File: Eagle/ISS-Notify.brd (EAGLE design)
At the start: 63.5 x 63.5 mm, 54 parts, among them J1 AVRISP, J2 JST2, J3 PROTOSPACE2, SW1 9077-1, SW2 SWITCH, U1 ATMEGA32U4, U2 MCP7940N, U3 TPS63001, U4 MCP73811, U5 TLC5971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

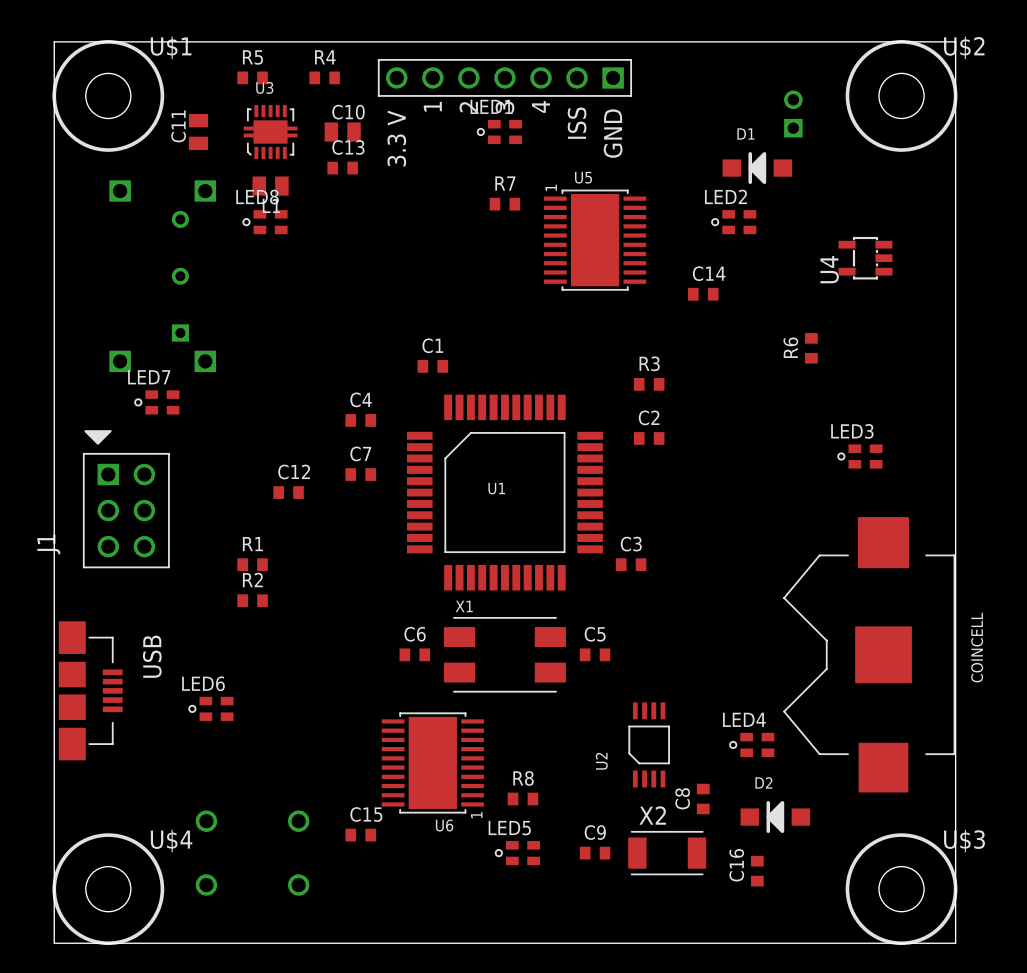
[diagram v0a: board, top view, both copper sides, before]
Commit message: power traces
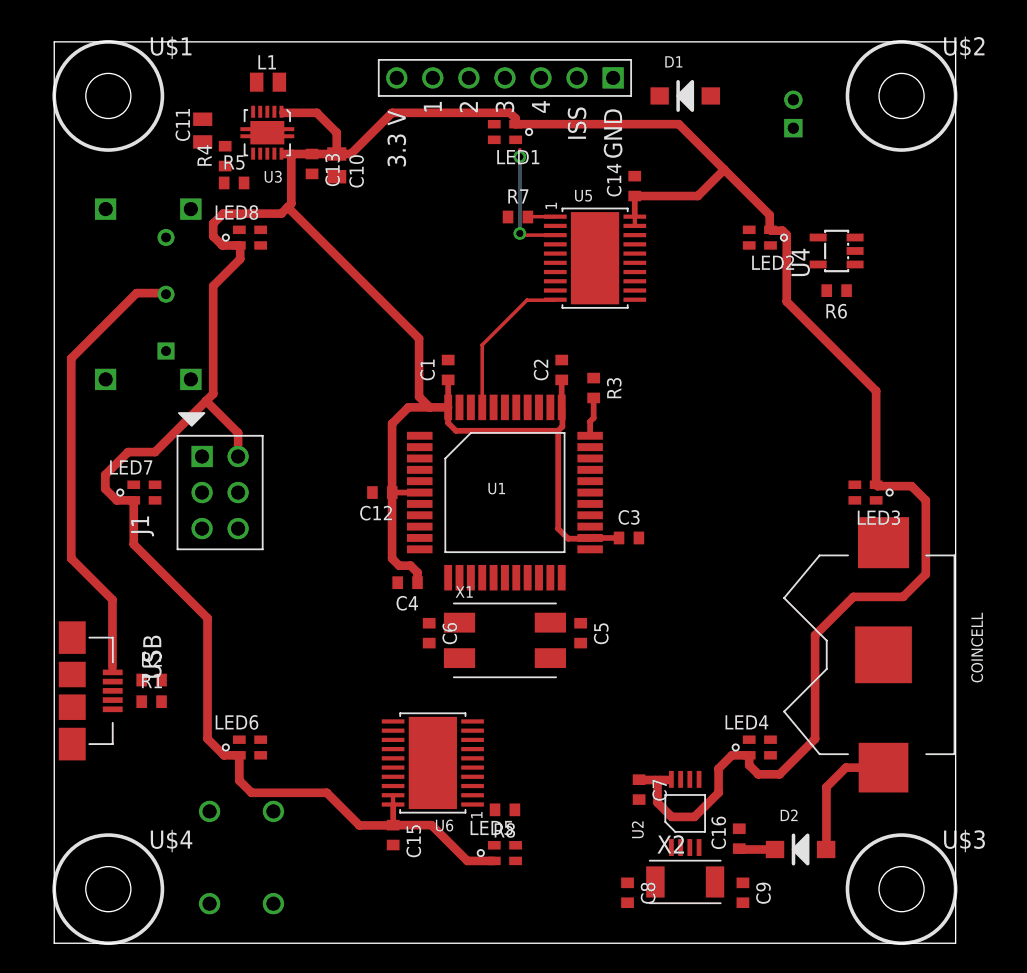
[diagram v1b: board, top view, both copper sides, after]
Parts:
- moved C7 29.6 mm to (41.2, 10.8), turned to 270 degrees
- moved R1 12.0 mm to (6.86, 17.0)
- moved C4 11.9 mm to (24.9, 25.4), turned to 180 degrees
- moved C9 10.8 mm to (48.5, 3.56), turned to 270 degrees
- moved R2 9.04 mm to (6.86, 18.5)
- moved C14 9.02 mm to (40.9, 53.3), turned to 90 degrees
- moved R4 8.92 mm to (12.0, 55.5), turned to 90 degrees
- moved C8 8.49 mm to (40.4, 3.56), turned to 270 degrees
- moved C2 7.83 mm to (35.8, 40.4), turned to 90 degrees
- moved R5 7.51 mm to (12.7, 53.6)
- moved L1 7.32 mm to (15.1, 60.7), turned to 0 degrees
- moved D1 7.18 mm to (44.5, 59.7)
- moved J1 6.73 mm to (11.7, 31.8)
- moved C12 6.60 mm to (23.1, 31.8), turned to 180 degrees
- moved LED7 6.48 mm to (6.35, 31.8)
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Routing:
- net VCC: track 0.00 -> 274.0 mm
- net VUSB: track 0.00 -> 31.9 mm
- net LED_CLK: track 0.00 -> 10.9 mm
- net N$11: track 0.00 -> 8.99 mm
- net N$22: track 0.00 -> 8.45 mm, vias 0 -> 2
- net N$42: track 0.00 -> 2.77 mm
- net N$15: track 0.00 -> 2.54 mm
- net N$17: track 0.00 -> 1.94 mm

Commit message: basic layout
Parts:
- moved C5 10.9 mm to (26.2, 21.0), turned to 90 degrees
- moved C6 10.9 mm to (37.3, 21.8)
- moved D1 2.02 mm to (46.5, 59.4)
- moved D2 1.50 mm to (52.7, 8.10)
- moved C16 1.40 mm to (48.4, 8.77)
- moved J1 1.08 mm to (12.7, 31.4)
- moved R7 1.04 mm to (33.4, 51.9), turned to 270 degrees
- moved R8 0.83 mm to (31.0, 9.05), turned to 90 degrees
- moved R6 0.60 mm to (54.5, 46.0)
- moved R1 0.45 mm to (7.06, 17.4)
- moved R2 0.45 mm to (7.06, 18.9)
- moved USB 0.20 mm to (1.47, 17.8)
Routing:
- net N$29: track 0.00 -> 47.7 mm, vias 0 -> 2
- net N$39: track 0.00 -> 45.5 mm, vias 0 -> 2
- net N$41: track 0.00 -> 44.9 mm, vias 0 -> 2
- net N$40: track 0.00 -> 44.9 mm, vias 0 -> 2
- net N$14: track 0.00 -> 44.7 mm, vias 0 -> 2
- net RESET: track 0.00 -> 43.9 mm
- net N$28: track 0.00 -> 43.9 mm, vias 0 -> 2
- net N$27: track 0.00 -> 42.3 mm, vias 0 -> 2
- net N$13: track 0.00 -> 40.5 mm, vias 0 -> 2
- net D-: track 0.00 -> 36.5 mm, vias 0 -> 4
- net N$30: track 0.00 -> 36.4 mm, vias 0 -> 2
- net D+: track 0.00 -> 35.4 mm, vias 0 -> 4
- net N$19: track 0.00 -> 34.1 mm, vias 0 -> 2
- net N$25: track 0.00 -> 33.1 mm, vias 0 -> 2
- net N$37: track 0.00 -> 32.2 mm, vias 0 -> 2
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
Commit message: pre-ground plane
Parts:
- moved R5 2.30 mm to (14.7, 52.5), turned to 180 degrees
- moved R4 2.28 mm to (12.6, 53.2)
- moved D1 1.60 mm to (47.8, 58.5), turned to 90 degrees
- moved C11 0.72 mm to (9.86, 56.9)
- moved C5 0.30 mm to (26.2, 20.7)
- moved J3 0.30 mm to (31.8, 61.3)
- moved X1 0.20 mm to (31.8, 21.1)
- moved C6 0.10 mm to (37.3, 21.7)
- moved L1 0.10 mm to (15.1, 60.6)
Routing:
- net VIN: track 0.00 -> 60.2 mm, vias 0 -> 4
- net VUSB: track 50.4 -> 90.8 mm, vias 0 -> 4
- net N$34: track 0.00 -> 36.9 mm, vias 0 -> 2
- net ISS: track 0.00 -> 32.0 mm, vias 0 -> 1
- net PF4: track 0.00 -> 26.2 mm, vias 0 -> 1
- net PF6: track 0.00 -> 25.5 mm, vias 0 -> 1
- net PF5: track 0.00 -> 25.4 mm, vias 0 -> 1
- net PF7: track 0.00 -> 24.7 mm, vias 0 -> 1
- net N$3: track 0.00 -> 4.63 mm
- net LED_DATA: track 11.4 -> 13.8 mm
- net N$2: track 0.00 -> 2.28 mm
- net N$1: track 0.00 -> 2.20 mm
- net VCC: track 281.9 -> 283.6 mm
- net GND: track 0.00 -> 1.48 mm
- net VBAT: track 16.3 -> 17.2 mm

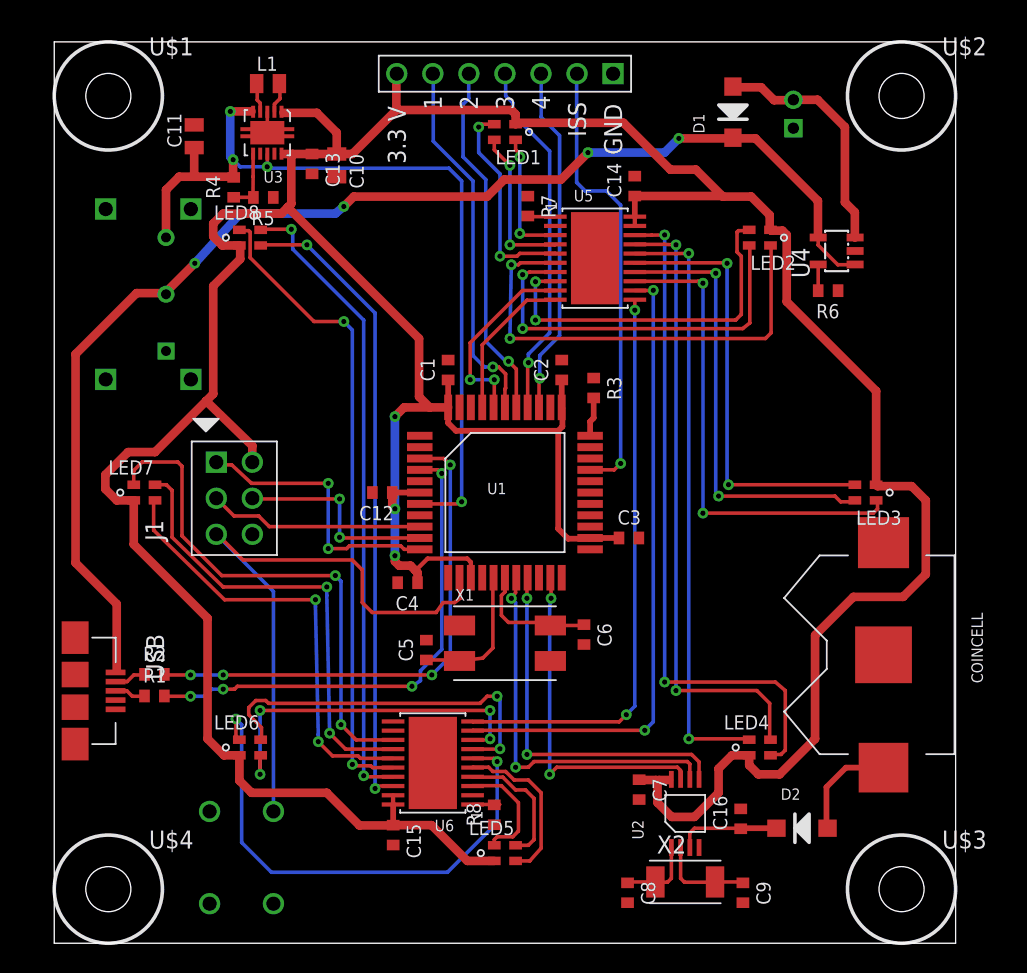
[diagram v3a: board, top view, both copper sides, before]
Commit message: Ground plane fill
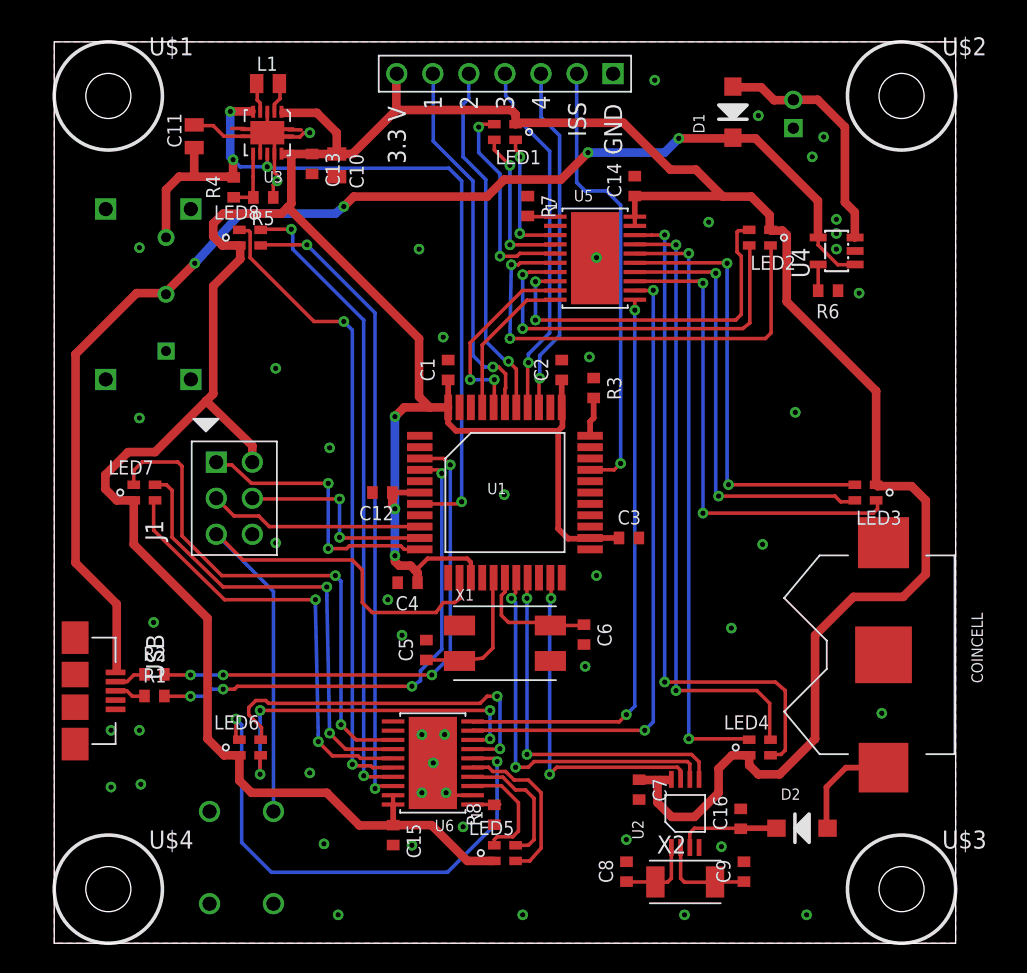
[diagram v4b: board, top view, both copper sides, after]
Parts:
- moved C8 1.49 mm to (40.3, 5.04), turned to 90 degrees
- moved C9 1.49 mm to (48.6, 5.04), turned to 90 degrees
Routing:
- net GND: track 1.48 -> 21.1 mm, vias 0 -> 49
- added copper zone on layer 1, net GND
- added copper zone on layer 16, net GND

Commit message: minor library updates, thermal pad under LiPo charger
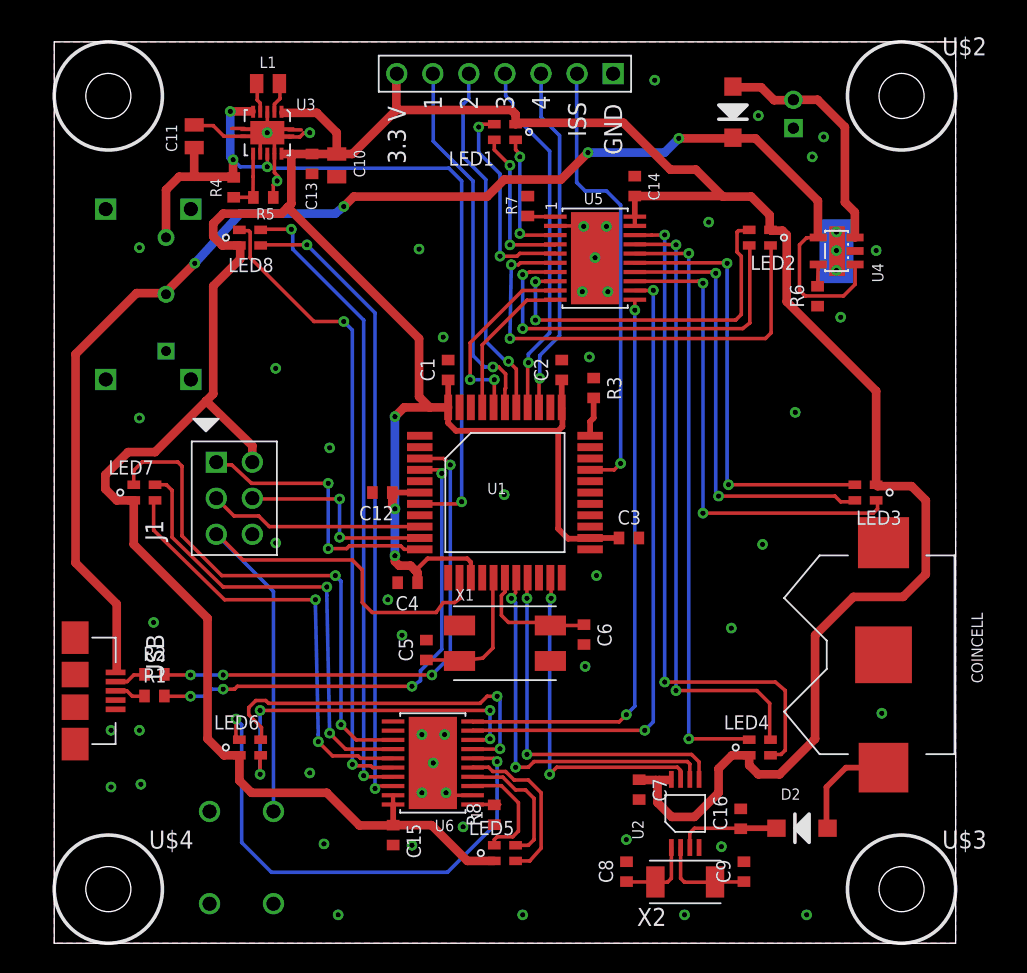
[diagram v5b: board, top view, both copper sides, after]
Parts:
- moved R6 0.84 mm to (53.8, 45.6), turned to 90 degrees
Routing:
- net VUSB: track 90.8 -> 97.6 mm
- net GND: track 21.1 -> 23.1 mm, vias 49 -> 52

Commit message: screen layer cleaned up
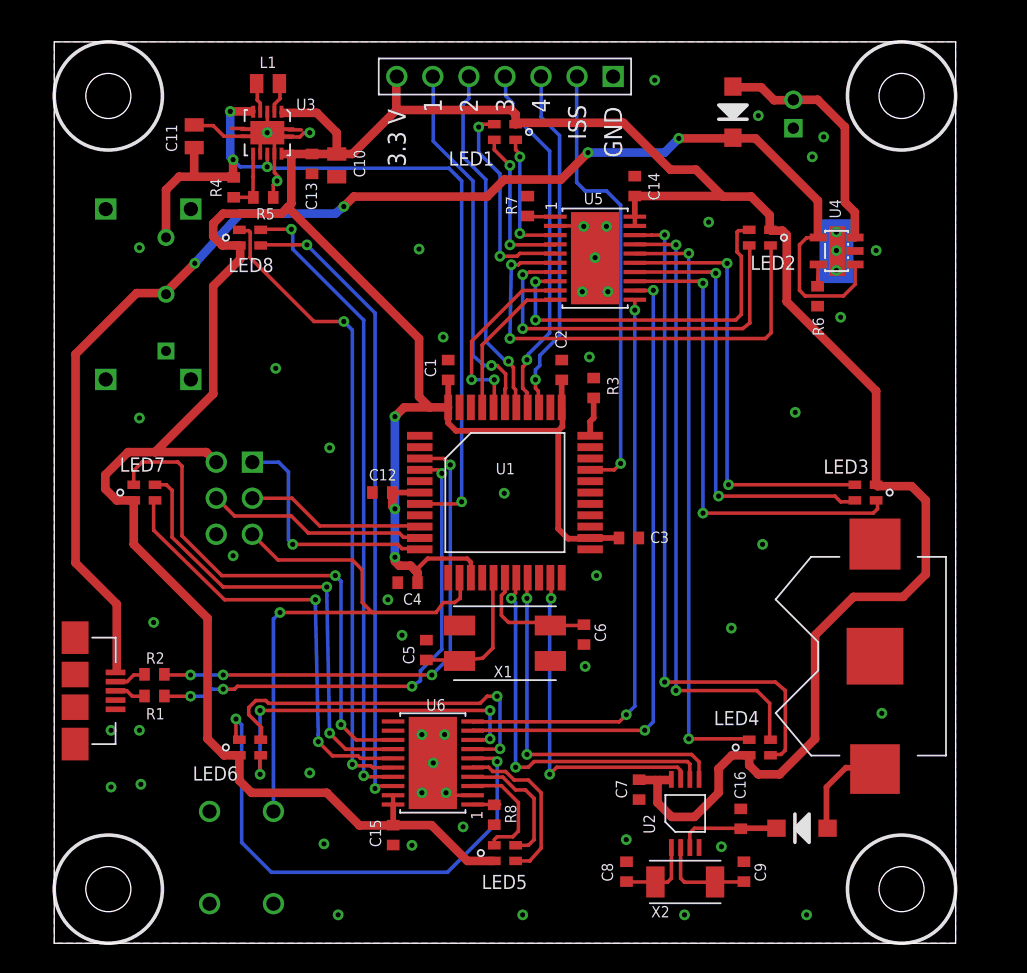
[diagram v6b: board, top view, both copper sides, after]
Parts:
- moved COINCELL 0.61 mm to (57.8, 20.2)
- moved J3 0.20 mm to (31.8, 61.1)
- flipped J1 to the bottom
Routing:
- net RESET: track 43.9 -> 40.9 mm, vias 0 -> 1
- net MISO: track 19.7 -> 17.2 mm, vias 2 -> 1
- net SCLK: track 15.2 -> 12.6 mm
- net VCC: track 283.6 -> 282.7 mm
- net MOSI: track 14.5 -> 15.5 mm, vias 2 -> 0
- net N$11: track 7.51 -> 6.91 mm
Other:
- board text added: "BATTERY"
